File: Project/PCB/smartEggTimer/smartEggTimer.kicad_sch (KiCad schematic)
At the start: 42 parts, among them J1 Conn_01x05_Pin, J2 Conn_01x02_Pin, J3 Conn_01x02_Pin, J4 Conn_01x02_Pin, J5 Conn_01x02_Socket, J6 Conn_01x02_Socket, J7 Conn_01x02_Socket, SW1 SW_Push_Dual, SW2 RotaryEncoder, SW3 SW_Push_Dual, SW4 SW_Push_Dual, SW5 SW_Push_Dual, SW6 SW_Push_Dual, SW7 SW_SPDT, U1 STM32F103RET6, U2 XC6206P332MR-G

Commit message: corrections and refinements for the schematic
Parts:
- removed J4: Conn_01x02_Pin, symbol Connector:Conn_01x02_Pin
- removed J7: Conn_01x02_Socket, symbol Connector:Conn_01x02_Socket
- removed U2: XC6206P332MR-G, Package_TO_SOT_SMD:SOT-23-3, symbol Regulator_Linear:XC6206PxxxMR
- added C12, C13: 10n, Capacitor_SMD:C_0805_2012Metric, symbol Device:C
- added C14: 100n, Capacitor_SMD:C_0402_1005Metric, symbol Device:C
- added C15, C16, C17, C18: 1u, Capacitor_SMD:C_0603_1608Metric, symbol Device:C
- added J4: Conn_01x06_Pin, symbol Connector:Conn_01x06_Pin
- added J7: Conn_01x03_Pin, Connector_PinHeader_2.54mm:PinHeader_1x03_P2.54mm_Vertical, symbol Connector:Conn_01x03_Pin
- added Q1: STP60NF06L, Package_TO_SOT_THT:TO-220-3_Vertical, symbol Simulation_SPICE:NMOS
- added R11, R16, R18, R20, R9: 10k, Resistor_SMD:R_0402_1005Metric, symbol Device:R
- added R12, R13: 1M, Resistor_SMD:R_0402_1005Metric, symbol Device:R
- added R15, R17, R19, R21: 22k, Resistor_SMD:R_0402_1005Metric, symbol Device:R
- added R3: 1k, Resistor_SMD:R_0402_1005Metric, symbol Device:R
- added R5: 100, Resistor_SMD:R_0402_1005Metric, symbol Device:R
- added U3: AP7361C-33E, Package_TO_SOT_SMD:SOT-223-3_TabPin2, symbol Regulator_Linear:AP7361C-33E
- C1: renamed from C6; footprint (none) -> Capacitor_SMD:C_0603_1608Metric
- C10: renamed from C11; value 1u -> 4u7; footprint (none) -> Capacitor_SMD:C_0603_1608Metric
- C11: renamed from C10; value 1u -> 4u7; footprint (none) -> Capacitor_SMD:C_0603_1608Metric
- C2: renamed from C5; value 100nF -> 100n; footprint (none) -> Capacitor_SMD:C_0402_1005Metric
- C3: renamed from C4; value 100nF -> 100n; footprint (none) -> Capacitor_SMD:C_0402_1005Metric
- C4: renamed from C3; value 100nF -> 100n; footprint (none) -> Capacitor_SMD:C_0402_1005Metric
- C5: renamed from C1; value 100nF -> 100n; footprint (none) -> Capacitor_SMD:C_0402_1005Metric
- C6: renamed from C2; value 100nF -> 100n; footprint (none) -> Capacitor_SMD:C_0402_1005Metric
- C7: value 10nF -> 10n; footprint (none) -> Capacitor_SMD:C_0805_2012Metric
- C8, C9: value 1uF -> 1u; footprint (none) -> Capacitor_SMD:C_0603_1608Metric
- DFPlayerMini1: footprint (none) -> custom-parts:DFplayer-Mini
- FB1: footprint (none) -> Inductor_SMD:L_0603_1608Metric
- H1, H2: footprint (none) -> MountingHole:MountingHole_4.3mm_M4
- H3, H8: footprint (none) -> MountingHole:MountingHole_4.3mm_M4_DIN965
- J1: footprint (none) -> Connector_PinHeader_2.54mm:PinHeader_1x05_P2.54mm_Vertical
- J2, J3: footprint (none) -> Connector_PinHeader_2.54mm:PinHeader_1x01_P2.54mm_Vertical
- J5, J6: footprint (none) -> Connector_PinHeader_2.54mm:PinHeader_1x02_P2.54mm_Vertical
- OLED-15W-C1: footprint (none) -> Connector_PinSocket_2.54mm:PinSocket_1x07_P2.54mm_Vertical
- R1, R2, R6, R7: footprint (none) -> Resistor_SMD:R_0402_1005Metric
- R10: renamed from R3; value R -> 10k; footprint (none) -> Resistor_SMD:R_0402_1005Metric
- R14: renamed from R5; value 4k7 -> 10k; footprint (none) -> Resistor_SMD:R_0402_1005Metric
- R4: value R -> 100k; footprint (none) -> Resistor_SMD:R_0402_1005Metric
- R8: value 4k7 -> 10k; footprint (none) -> Resistor_SMD:R_0402_1005Metric
- SW1: footprint (none) -> Button_Switch_THT:SW_PUSH_6mm_H9.5mm
- SW2: value RotaryEncoder -> EC12E24204A2; footprint (none) -> Rotary_Encoder:RotaryEncoder_Alps_EC12E_Vertical_H20mm
- SW3, SW4, SW5, SW6: footprint (none) -> Button_Switch_THT:SW_PUSH_6mm_H13mm
- SW7: footprint (none) -> Button_Switch_THT:SW_Slide_SPDT_Angled_CK_OS102011MA1Q
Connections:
- net +3.3V: now also R8.1, U1.1 (VBAT), U1.19 (VDD), U1.32 (VDD), U1.48 (VDD), U1.64 (VDD), J4.1 (Pin_1), J4.2 (Pin_2), J4.5 (Pin_5), J7.2 (Pin_2), R11.1, R16.2, R18.2, R20.2, U3.3 (VO); no longer DFPlayerMini1. (VCC), R10.2, R4.2, R8.2
- net BOOT0: now also R2.2, U1.60 (BOOT0)
- net Battery-SW: now also DFPlayerMini1. (VCC), R12.2, U3.1 (VI)
- net Button_1: now also C15.1, R15.1; no longer R14.1, SW3.1, SW3.2
- net Button_2: now also C17.1, R19.1; no longer R6.1, SW4.1, SW4.2
- net Button_3: now also C16.1, R17.1; no longer R7.1, SW5.1, SW5.2
- net Button_4: now also C18.1, R21.1
- net GND: now also R4.2, C12.2, C13.1, C14.2, C15.2, C16.2, C17.2, C18.2, J4.6 (Pin_6), J7.1 (Pin_1), Q1.3 (S), R13.1, U3.2 (GND); no longer DFPlayerMini1. (VCC), U1.1 (VBAT), U1.19 (VDD), U1.32 (VDD), U1.48 (VDD), U1.64 (VDD)
- net I2C1_SDA: now also R6.1, J4.3 (Pin_3)
- net I2C_SCL: now also R7.1, J4.4 (Pin_4)
- net LED: now also J7.3 (Pin_3)
- net Rotary Encoder a: now also C12.1, R9.2; no longer R4.1, SW2.A
- net Rotary Encoder b: now also R10.2, C13.2; no longer R10.1, SW2.B
- net display_reset: now reaches OLED-15W-C1. (VCC)
- net display_reset: now also U1.55 (PB3)
- net UART2_RX: now reaches U1.17 (PA3)
- net UART2_RX: now also R3.2
- net UART2_TX: now reaches U1.20 (PA4)
- net UART2_TX: now also DFPlayerMini1. (VCC)
- net Battery_indicator: now reaches U1.23 (PA7)
- net Battery_indicator: now also C14.1, R12.1, R13.2
- net DFPlayer-On/Off switch: now reaches U1.26 (PB0)
- net DFPlayer-On/Off switch: now also R5.1
- removed net UART5_RX: DFPlayerMini1. (VCC), J3.1 (Pin_1), U1.54 (PD2)
- removed net UART5_TX: DFPlayerMini1. (VCC), J3.2 (Pin_2), U1.53 (PC12)
- new net: R15.2, SW3.2
- new net: R8.2, R9.1, SW2.A
- new net: DFPlayerMini1. (VCC), R3.1
- new net: R19.2, SW5.2
- new net: R16.1, SW4.1
- new net: R17.2, SW4.2
- new net: R18.1, SW5.1
- new net: R10.1, R11.2, SW2.B
- new net: R14.1, SW3.1
- new net: DFPlayerMini1. (VCC), Q1.1 (D)
- new net: Q1.2 (G), R4.1, R5.2
- new net: R20.1, SW6.1
- new net: R21.2, SW6.2
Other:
- note added: "(buttons soldered sepeately)"
- note added: "4.7uF input/output capacitors according to AP7361C's datasheet"
- note added: "7 Holes for display (display soldered manually)"
- note added: "Battery Indicator"
- note added: "Condensator and resistor for hardware debouncing"
- note added: "DFPlayer mini"
- note added: "Digital LED"
- note added: "M4"
- note added: "Microcontroller"
- note added: "Mounting Holes"
- note added: "On/Off switch (soldered separately)"
- note added: "Push Buttons"
- note added: "SWD Debug/Programming Interface"
- note added: "SmartEggTimer"
- note added: "TODO: select STM pins for additional UART port"
- note added: "The DFPlayer can be used with 3,2 - 5V, so we can connect the chip directly to our battery"
- note added: "The DFPlayer has a high standby current of about 20mA, so an NMOS is used to turn off the DFPlayer when it is not needed"
- note added: "Using I2C: - DIN is connected to control pin SDA, - CLK is connected to control pin SCL, - CS and DC are not connected. NOTE: BS1 and BS2 on the display controller have to connected to 1, so two 0 Ohm resistors have to be moved"
- note added: "Waveshare 1.5inch OLED Module"
- note added: "additional resistors and capacitors for hardware debouncing"
- note added: "connected to DS3231 module"
- note added: "optional extension"
- note added: "optional extension to connect a pressure sensor, e.g. BMP280"
- note added: "to GND to boot from main flash memory"
- note added: "to measure the voltage (i.e. the charge) of the battery"
- note added: "voltage divider to half the battery output voltage for the STM32 (max. 3.3V) high resistance of 1M chosen to limit the constant current flow from Battery-SW to GND capacitor acts as "buffer" and will be charged between measurements"
- note removed: "7 Holes for display (to solder the display)"
- note removed: "Chip selection, low active @todo Data/Command selection (high for data, low for command) @todo Reset signal, low active @todo"
- note removed: "DF player (Mounting holes only)"
- note removed: "Debug 3.3v power supply (wenn used with swd)"
- note removed: "Holes for buttons"
- note removed: "Mounting"
- note removed: "On/off switch (soldered separately)"
- note removed: "SWDIO + SWDCLk"
- note removed: "evtl. auch einfach auch nur Löcher zum löten?"
- note removed: "to GND to boot from ? (user Flash?)"
- moved on the sheet: C1, C10, C11, C2, C3, C4, C5, C6, C7, C8, C9, FB1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

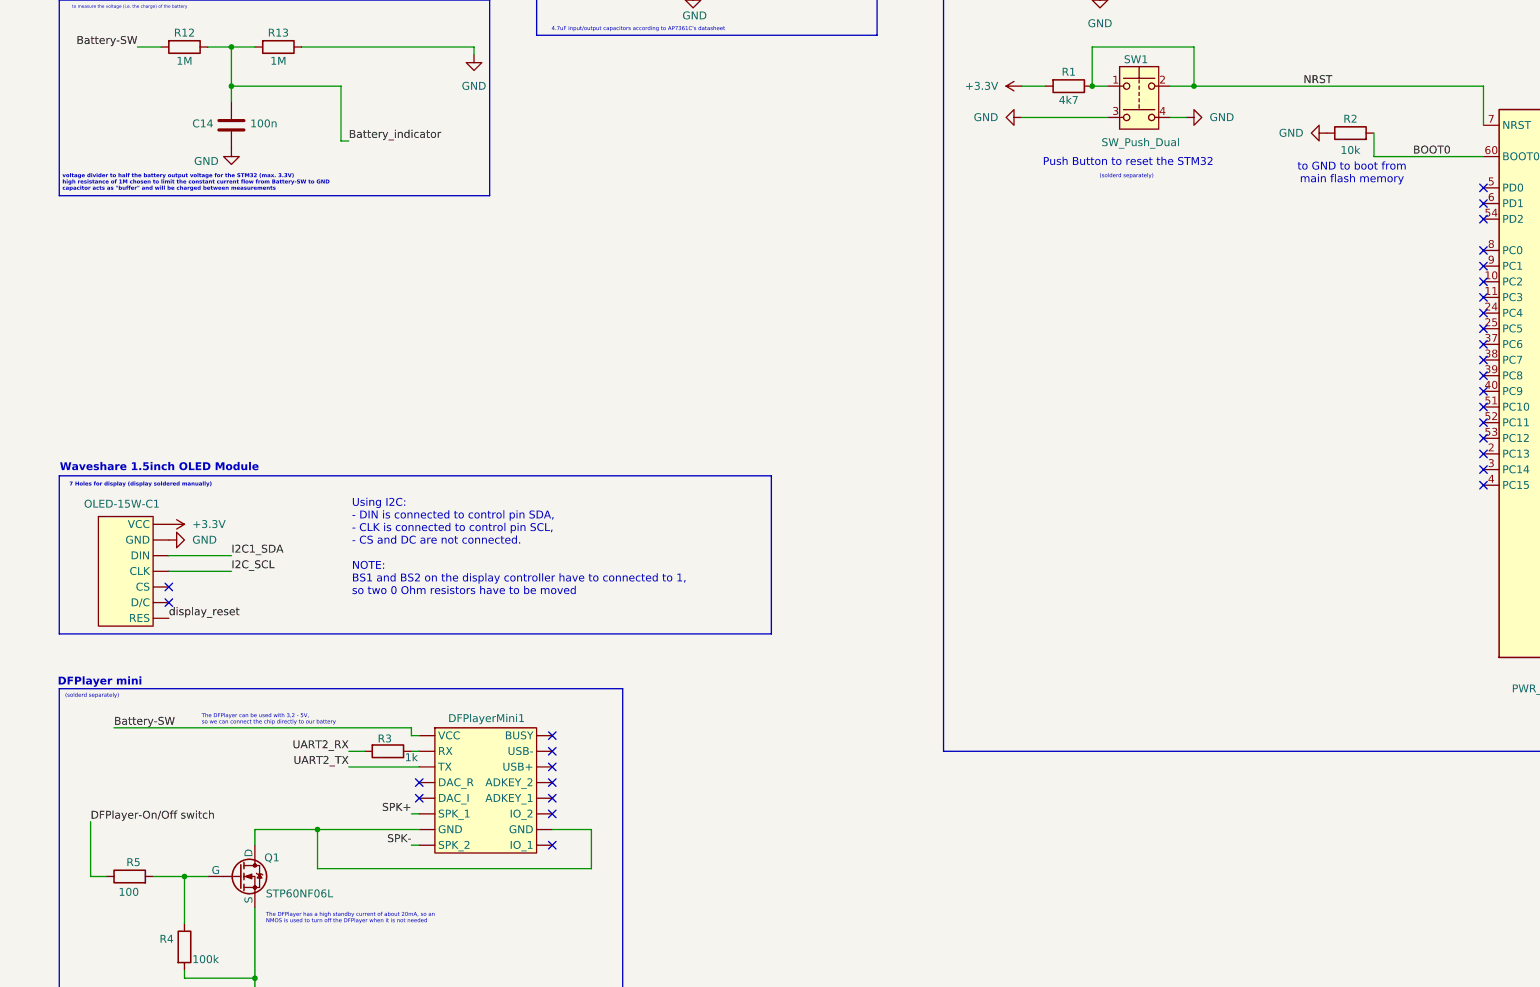
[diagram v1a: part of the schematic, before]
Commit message: add DAC out
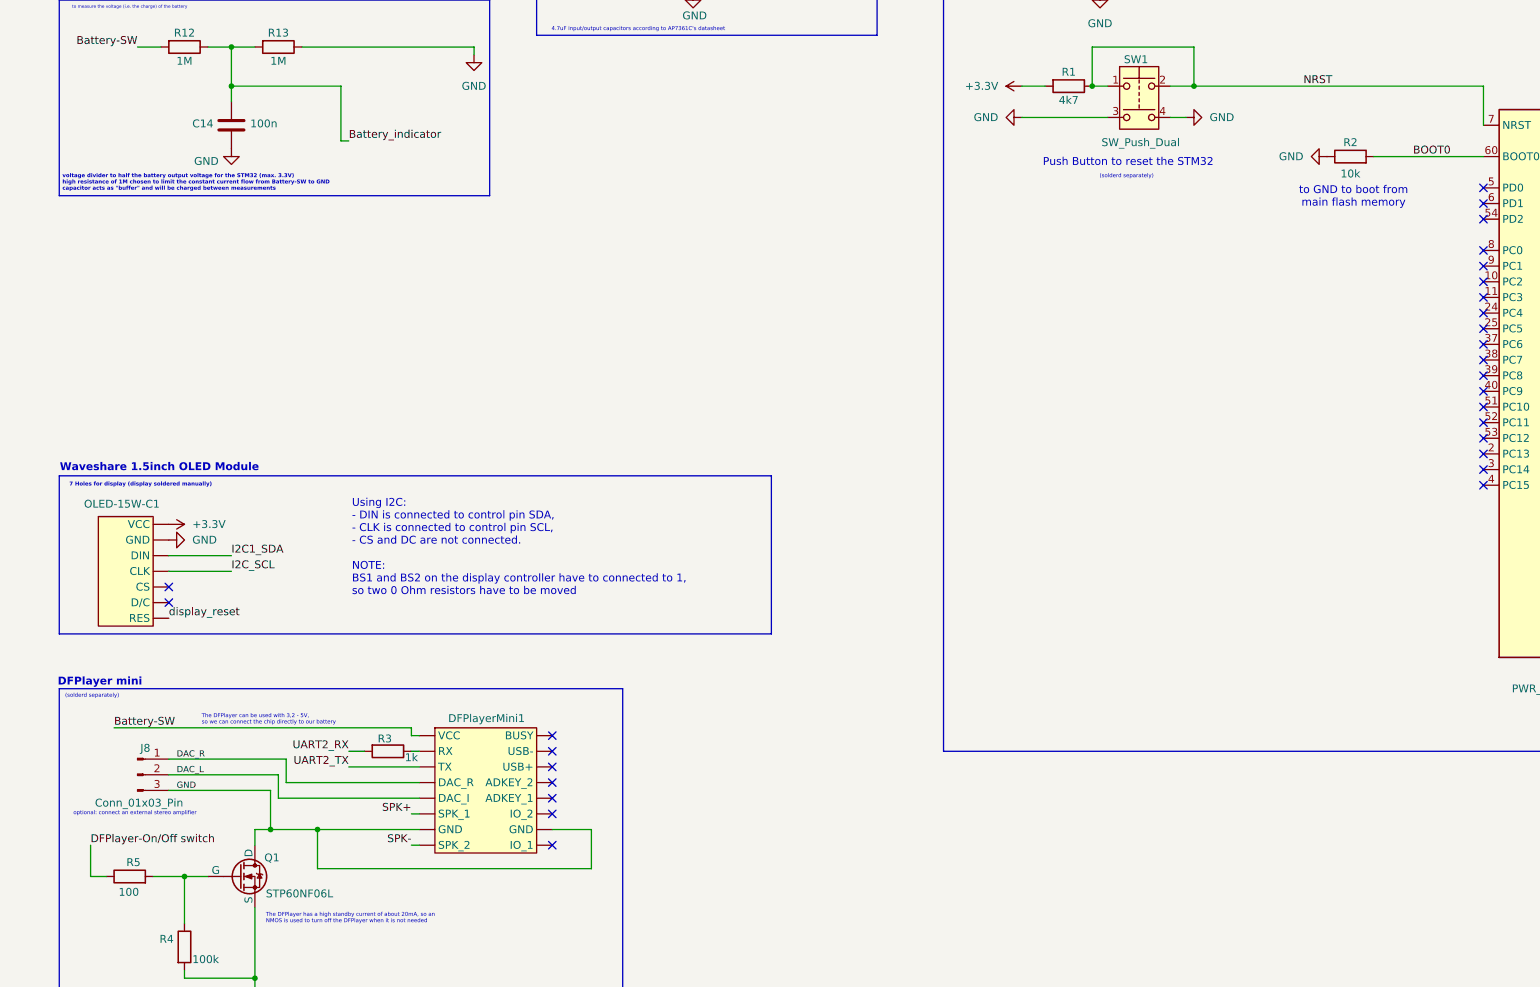
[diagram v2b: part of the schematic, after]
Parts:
- added J8: Conn_01x03_Pin, symbol Connector:Conn_01x03_Pin
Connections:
- net GND: now also DFPlayerMini1. (VCC), Q1.1 (D), J8.3 (Pin_3)
- new net DAC_L: DFPlayerMini1. (VCC), J8.2 (Pin_2)
- new net DAC_R: DFPlayerMini1. (VCC), J8.1 (Pin_1)
- no-connect marks 50 -> 48
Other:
- note added: "optional: connect an external stereo amplifier"
- moved on the sheet: R2
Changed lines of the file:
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@@
 		(color 0 0 0 0)
 	)
+	(junction
+		(at 52.07 186.69)
+		(diameter 0)
+		(color 0 0 0 0)
+	)
 	(no_connect
 		(at 248.92 107.95)
@@
 	)
 	(no_connect
-		(at 76.2 181.61)
-	)
-	(no_connect
 		(at 248.92 105.41)
 	)
@@
 	)
 	(no_connect
-		(at 76.2 179.07)
-	)
-	(no_connect
 		(at 284.48 135.89)
 	)
@@
 	(wire
 		(pts
+			(xy 22.86 189.23) (xy 22.86 194.31)
+		)
+		(stroke
+			(width 0)
+			(type default)
+		)
+	)
+	(wire
+		(pts
 			(xy 49.53 189.23) (xy 49.53 186.69)
 		)
@@
 	(wire
 		(pts
-			(xy 231.14 73.66) (xy 231.14 77.47)
-		)
-		(stroke
-			(width 0)
-			(type default)
-		)
-	)
-	(wire
-		(pts
 			(xy 186.69 49.53) (xy 186.69 50.8)
 		)
@@
 	(wire
 		(pts
+			(xy 54.61 179.07) (xy 76.2 179.07)
+		)
+		(stroke
+			(width 0)
+			(type default)
+		)
+	)
+	(wire
+		(pts
 			(xy 119.38 255.27) (xy 121.92 255.27)
 		)
@@
 	(wire
 		(pts
+			(xy 76.2 181.61) (xy 53.34 181.61)
+		)
+		(stroke
+			(width 0)
+			(type default)
+		)
+	)
+	(wire
+		(pts
 			(xy 85.09 59.69) (xy 85.09 60.96)
 		)
@@
 	(wire
 		(pts
-			(xy 49.53 186.69) (xy 59.69 186.69)
+			(xy 49.53 186.69) (xy 52.07 186.69)
 		)
 		(stroke
@@
 	(wire
 		(pts
-			(xy 119.38 236.22) (xy 121.92 236.22)
+			(xy 35.56 175.26) (xy 54.61 175.26)
 		)
 		(stroke
@@
 	(wire
 		(pts
-			(xy 358.14 105.41) (xy 358.14 113.03)
+			(xy 119.38 236.22) (xy 121.92 236.22)
 		)
 		(stroke
@@
 	(wire
 		(pts
-			(xy 35.56 142.24) (xy 45.72 142.24)
+			(xy 358.14 105.41) (xy 358.14 113.03)
 		)
 		(stroke
@@
 	(wire
 		(pts
-			(xy 22.86 185.42) (xy 22.86 194.31)
+			(xy 35.56 142.24) (xy 45.72 142.24)
 		)
 		(stroke
@@
 	(wire
 		(pts
+			(xy 54.61 175.26) (xy 54.61 179.07)
+		)
+		(stroke
+			(width 0)
+			(type default)
+		)
+	)
+	(wire
+		(pts
 			(xy 284.48 133.35) (xy 302.26 133.35)
 		)
@@
 	(wire
 		(pts
+			(xy 35.56 177.8) (xy 53.34 177.8)
+		)
+		(stroke
+			(width 0)
+			(type default)
+		)
+	)
+	(wire
+		(pts
 			(xy 274.32 36.83) (xy 274.32 40.64)
 		)
@@
 	(wire
 		(pts
+			(xy 35.56 180.34) (xy 52.07 180.34)
+		)
+		(stroke
+			(width 0)
+			(type default)
+		)
+	)
+	(wire
+		(pts
 			(xy 354.33 115.57) (xy 363.22 115.57)
 		)
@@
 	(wire
 		(pts
+			(xy 52.07 186.69) (xy 59.69 186.69)
+		)
+		(stroke
+			(width 0)
+			(type default)
+		)
+	)
+	(wire
+		(pts
 			(xy 198.12 41.91) (xy 210.82 41.91)
 		)
@@
 	(wire
 		(pts
+			(xy 53.34 181.61) (xy 53.34 177.8)
+		)
+		(stroke
+			(width 0)
+			(type default)
+		)
+	)
+	(wire
+		(pts
+			(xy 52.07 180.34) (xy 52.07 186.69)
+		)
+		(stroke
+			(width 0)
+			(type default)
+		)
+	)
+	(wire
+		(pts
 			(xy 198.12 71.12) (xy 200.66 71.12)
 		)
@@
 		)
 	)
+	(text "optional: connect an external stereo amplifier"
+		(exclude_from_sim no)
+		(at 20.066 184.15 0)
+		(effects
+			(font
+				(size 0.635 0.635)
+			)
+			(justify left)
+		)
+	)
 	(text "M4"
 		(exclude_from_sim no)
@@
 	(text "to GND to boot from\nmain flash memory"
 		(exclude_from_sim no)
-		(at 227.584 80.264 0)
+		(at 227.838 84.074 0)
 		(effects
 			(font
@@
 		)
 	)
+	(label "DAC_L"
+		(at 36.83 177.8 0)
+		(fields_autoplaced yes)
+		(effects
+			(font
+				(size 1 1)
+			)
+			(justify left bottom)
+		)
+	)
 	(label "Rotary Encoder a"
 		(at 284.48 95.25 0)
@@
 		)
 	)
+	(label "DAC_R"
+		(at 36.83 175.26 0)
+		(fields_autoplaced yes)
+		(effects
+			(font
+				(size 1 1)
+			)
+			(justify left bottom)
+		)
+	)
 	(label "DFPlayer-On{slash}Off switch"
-		(at 22.86 185.42 0)
+		(at 22.86 189.23 0)
 		(fields_autoplaced yes)
 		(effects
@@
 		)
 	)
+	(label "GND"
+		(at 36.83 180.34 0)
+		(fields_autoplaced yes)
+		(effects
+			(font
+				(size 1 1)
+			)
+			(justify left bottom)
+		)
+	)
 	(label "Bat+"
 		(at 31.75 30.48 180)
@@
 	)
 	(symbol
+		(lib_id "Connector:Conn_01x03_Pin")
+		(at 30.48 177.8 0)
+		(unit 1)
+		(exclude_from_sim no)
+		(in_bom yes)
+		(on_board yes)
+		(dnp no)
+		(property "Reference" "J8"
+			(at 31.75 173.482 0)
+			(effects
+				(font
+					(size 1.27 1.27)
+				)
+			)
+		)
+		(property "Value" "Conn_01x03_Pin"
+			(at 30.734 182.372 0)
+			(effects
+				(font
+					(size 1.27 1.27)
+				)
+			)
+		)
+		(property "Footprint" ""
+			(at 30.48 177.8 0)
+			(effects
+				(font
+					(size 1.27 1.27)
+				)
+				(hide yes)
+			)
+		)
+		(property "Datasheet" "~"
+			(at 30.48 177.8 0)
+			(effects
+				(font
+					(size 1.27 1.27)
+				)
+				(hide yes)
+			)
+		)
+		(property "Description" "Generic connector, single row, 01x03, script generated"
+			(at 30.48 177.8 0)
+			(effects
+				(font
+					(size 1.27 1.27)
+				)
+				(hide yes)
+			)
+		)
+		(pin "1"
+		)
+		(pin "2"
+		)
+		(pin "3"
+		)
+		(instances
+			(project ""
+				(path "/9fde6b9c-53fd-4f64-9761-84b01b75f921"
+					(reference "J8")
+					(unit 1)
+				)
+			)
+		)
+	)
+	(symbol
 		(lib_id "Device:R")
 		(at 138.43 236.22 270)
@@
 	(symbol
 		(lib_id "power:GND")
-		(at 223.52 73.66 270)
+		(at 223.52 77.47 270)
 		(unit 1)
 		(exclude_from_sim no)
@@
 		(fields_autoplaced yes)
 		(property "Reference" "#PWR011"
-			(at 217.17 73.66 0)
+			(at 217.17 77.47 0)
 			(effects
 				(font
@@
 		)
 		(property "Value" "GND"
-			(at 219.71 73.6599 90)
+			(at 219.71 77.4699 90)
 			(effects
 				(font
@@
 		)
 		(property "Footprint" ""
-			(at 223.52 73.66 0)
+			(at 223.52 77.47 0)
 			(effects
 				(font
@@
 		)
 		(property "Datasheet" ""
-			(at 223.52 73.66 0)
+			(at 223.52 77.47 0)
 			(effects
 				(font
@@
 		)
 		(property "Description" "Power symbol creates a global label with name \"GND\" , ground"
-			(at 223.52 73.66 0)
+			(at 223.52 77.47 0)
 			(effects
 				(font
@@
 	(symbol
 		(lib_id "Device:R")
-		(at 227.33 73.66 90)
+		(at 227.33 77.47 90)
 		(unit 1)
 		(exclude_from_sim no)
@@
 		(dnp no)
 		(property "Reference" "R2"
-			(at 227.33 71.374 90)
+			(at 227.33 75.184 90)
 			(effects
 				(font
@@
 		)
 		(property "Value" "10k"
-			(at 227.33 76.454 90)
+			(at 227.33 80.264 90)
 			(effects
 				(font
@@
 		)
 		(property "Footprint" "Resistor_SMD:R_0402_1005Metric"
-			(at 227.33 75.438 90)
+			(at 227.33 79.248 90)
 			(effects
 				(font
@@
 		)
 		(property "Datasheet" "~"
-			(at 227.33 73.66 0)
+			(at 227.33 77.47 0)
 			(effects
 				(font
@@
 		)
 		(property "Description" "Resistor"
-			(at 227.33 73.66 0)
+			(at 227.33 77.47 0)
 			(effects
 				(font

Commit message: add pin numbers for display
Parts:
- J2, J3: footprint Connector_PinHeader_2.54mm:PinHeader_1x01_P2.54mm_Vertical -> Connector_PinHeader_2.54mm:PinHeader_1x02_P2.54mm_Vertical
- J4: footprint (none) -> Connector_PinHeader_2.54mm:PinHeader_1x06_P2.54mm_Vertical
- J8: footprint (none) -> Connector_PinHeader_2.54mm:PinHeader_1x03_P2.54mm_Vertical
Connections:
- net +3.3V: now also OLED-15W-C1.1 (VCC); no longer OLED-15W-C1. (VCC)
- net GND: now also OLED-15W-C1.2 (GND); no longer DFPlayerMini1. (VCC), OLED-15W-C1. (VCC), Q1.1 (D)
- net I2C1_SDA: now also OLED-15W-C1.3 (DIN); no longer OLED-15W-C1. (VCC)
- net I2C_SCL: now also OLED-15W-C1.4 (CLK); no longer OLED-15W-C1. (VCC)
- net display_reset: now also OLED-15W-C1.7 (RES); no longer OLED-15W-C1. (VCC)
- new net: DFPlayerMini1. (VCC), Q1.1 (D)
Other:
- note added: "Audio out"
- moved on the sheet: J3, J4, J7
